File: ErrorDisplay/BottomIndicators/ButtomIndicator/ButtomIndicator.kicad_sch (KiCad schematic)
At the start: 10 parts

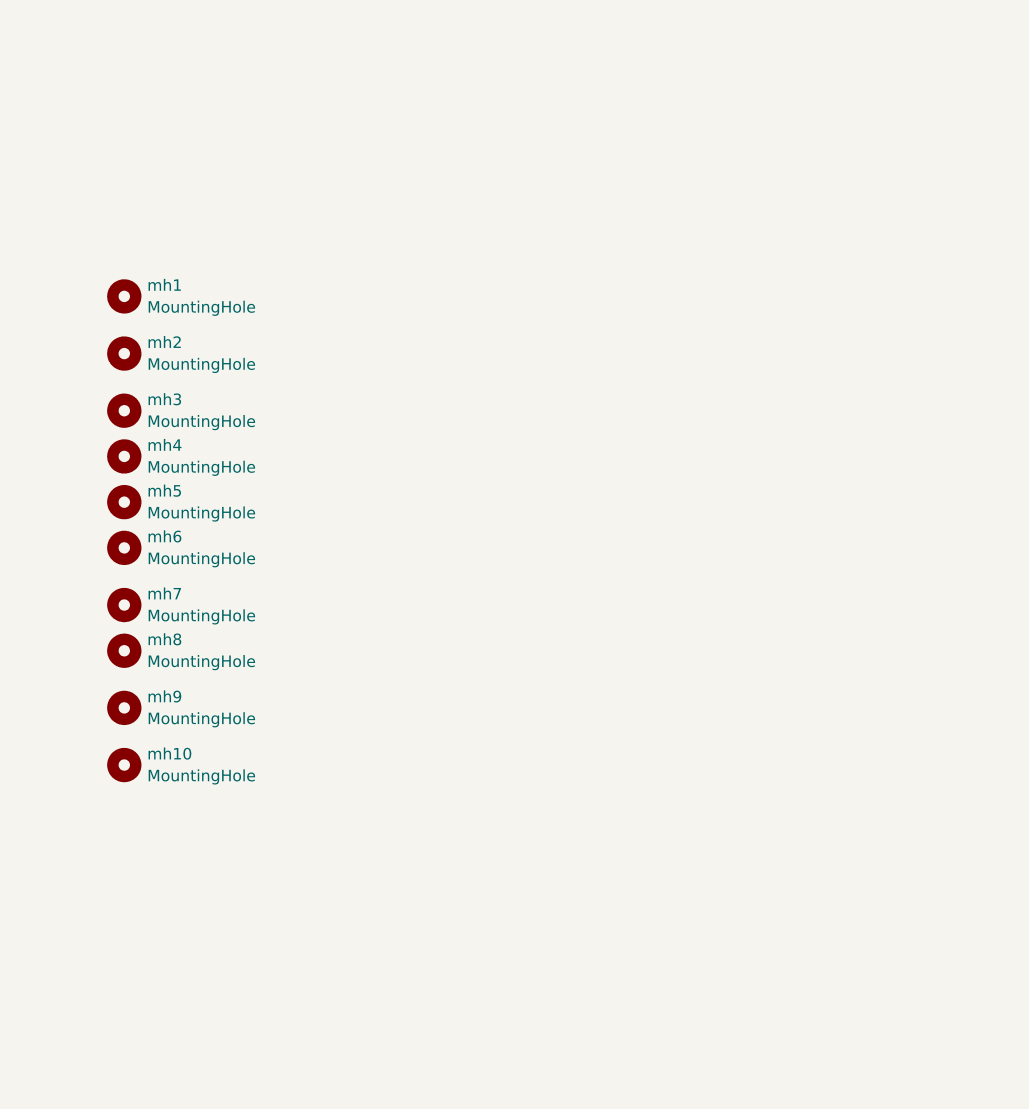
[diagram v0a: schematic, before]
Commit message: Placement and positioning of icons
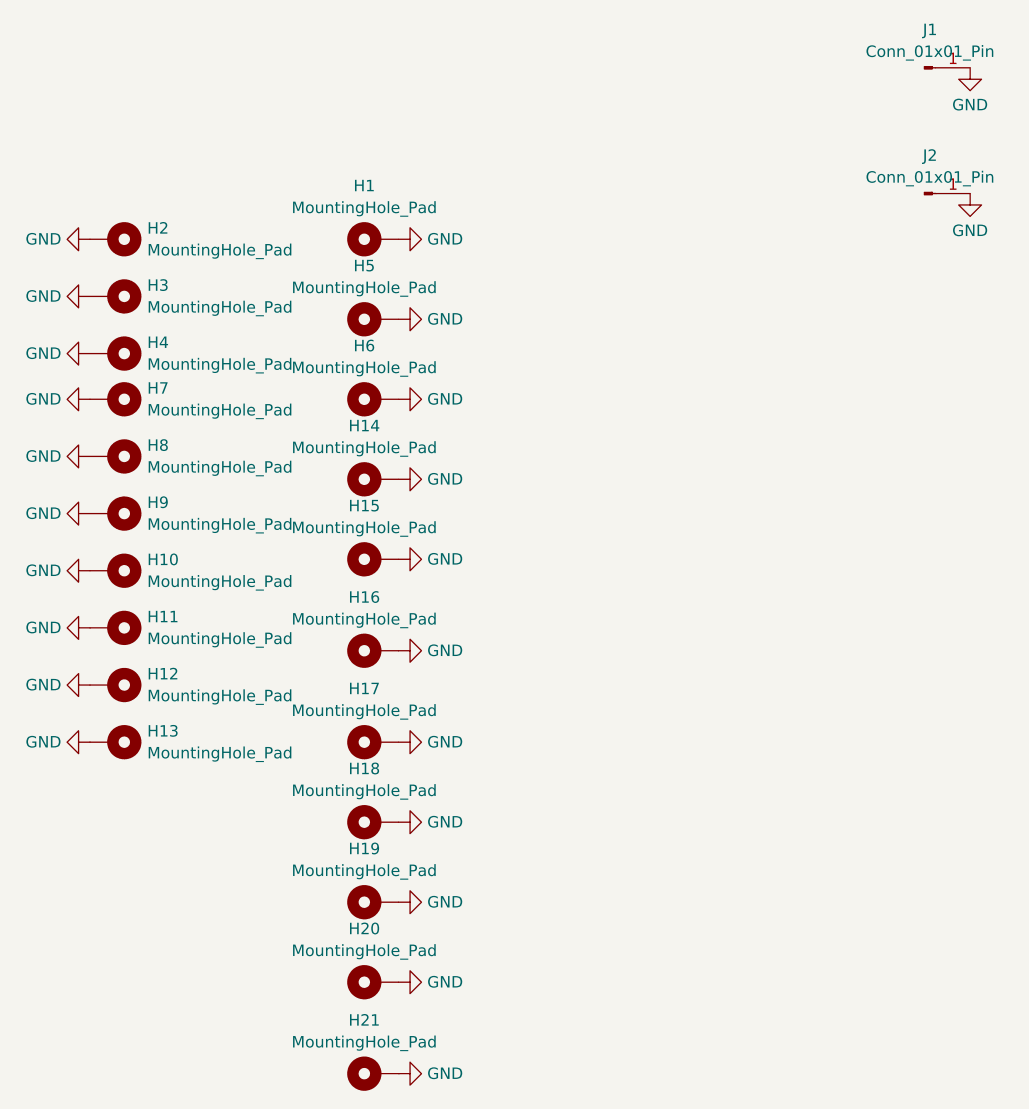
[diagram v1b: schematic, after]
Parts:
- removed mh1, mh10, mh2, mh3, mh4, mh5, mh6, mh7, mh8, mh9: MountingHole, Library:PlasticInsert, symbol Mechanical:MountingHole
- added H1: MountingHole_Pad, Library:brights, symbol Mechanical:MountingHole_Pad
- added H10, H11, H12, H13, H2, H3, H4, H7, H8, H9: MountingHole_Pad, Library:PlasticInsert, symbol Mechanical:MountingHole_Pad
- added H14: MountingHole_Pad, Library:lights, symbol Mechanical:MountingHole_Pad
- added H15, H17: MountingHole_Pad, Library:turn, symbol Mechanical:MountingHole_Pad
- added H16: MountingHole_Pad, Library:parking, symbol Mechanical:MountingHole_Pad
- added H18: MountingHole_Pad, Library:defrost, symbol Mechanical:MountingHole_Pad
- added H19: MountingHole_Pad, Library:thermals, symbol Mechanical:MountingHole_Pad
- added H20: MountingHole_Pad, Library:motorthermal, symbol Mechanical:MountingHole_Pad
- added H21: MountingHole_Pad, symbol Mechanical:MountingHole_Pad
- added H5: MountingHole_Pad, Library:buttbutt, symbol Mechanical:MountingHole_Pad
- added H6: MountingHole_Pad, Library:dickbutt_hv, symbol Mechanical:MountingHole_Pad
- added J1, J2: Conn_01x01_Pin, MountingHole:MountingHole_2.2mm_M2_DIN965_Pad, symbol Connector:Conn_01x01_Pin
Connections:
- new net GND: H1.1, H10.1, H11.1, H12.1, H13.1, H14.1, H15.1, H16.1, H17.1, H18.1, H19.1, H2.1, H20.1, H21.1, H3.1, H4.1, H5.1, H6.1, H7.1, H8.1, H9.1, J1.1 (Pin_1), J2.1 (Pin_1)

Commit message: Proper Layout
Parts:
- H21: footprint (none) -> Library:dickbutt_12
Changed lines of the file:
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@@
 			)
 		)
-		(property "Footprint" ""
+		(property "Footprint" "Library:dickbutt_12"
 			(at 125.73 157.48 0)
 			(effects
